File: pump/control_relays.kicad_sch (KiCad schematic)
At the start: 16 parts, among them K1 G5LE-1, K2 G5LE-1, Q1 PNP, Q2 PNP, U1 LTV-817S, U2 LTV-817S

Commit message: -:
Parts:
- D1: footprint Diode_SMD:D_MELF -> Diode_SMD:D_0805_2012Metric_Pad1.15x1.40mm_HandSolder
- D2: LCSC (none) -> C64898; PartNo SM4007PL -> (none)
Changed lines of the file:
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@@
 			)
 		)
-		(property "Footprint" "Diode_SMD:D_MELF"
+		(property "Footprint" "Diode_SMD:D_0805_2012Metric_Pad1.15x1.40mm_HandSolder"
 			(at 135.255 120.65 0)
 			(effects
@@
 			)
 		)
-		(property "Field7" ""
+		(property "LCSC" "C64898"
 			(at 139.7 57.15 90)
 			(effects
-				(font
-					(size 1.27 1.27)
-				)
-				(hide yes)
-			)
-		)
-		(property "PartNo" "SM4007PL"
-			(at 139.7 57.15 90)
-			(effects

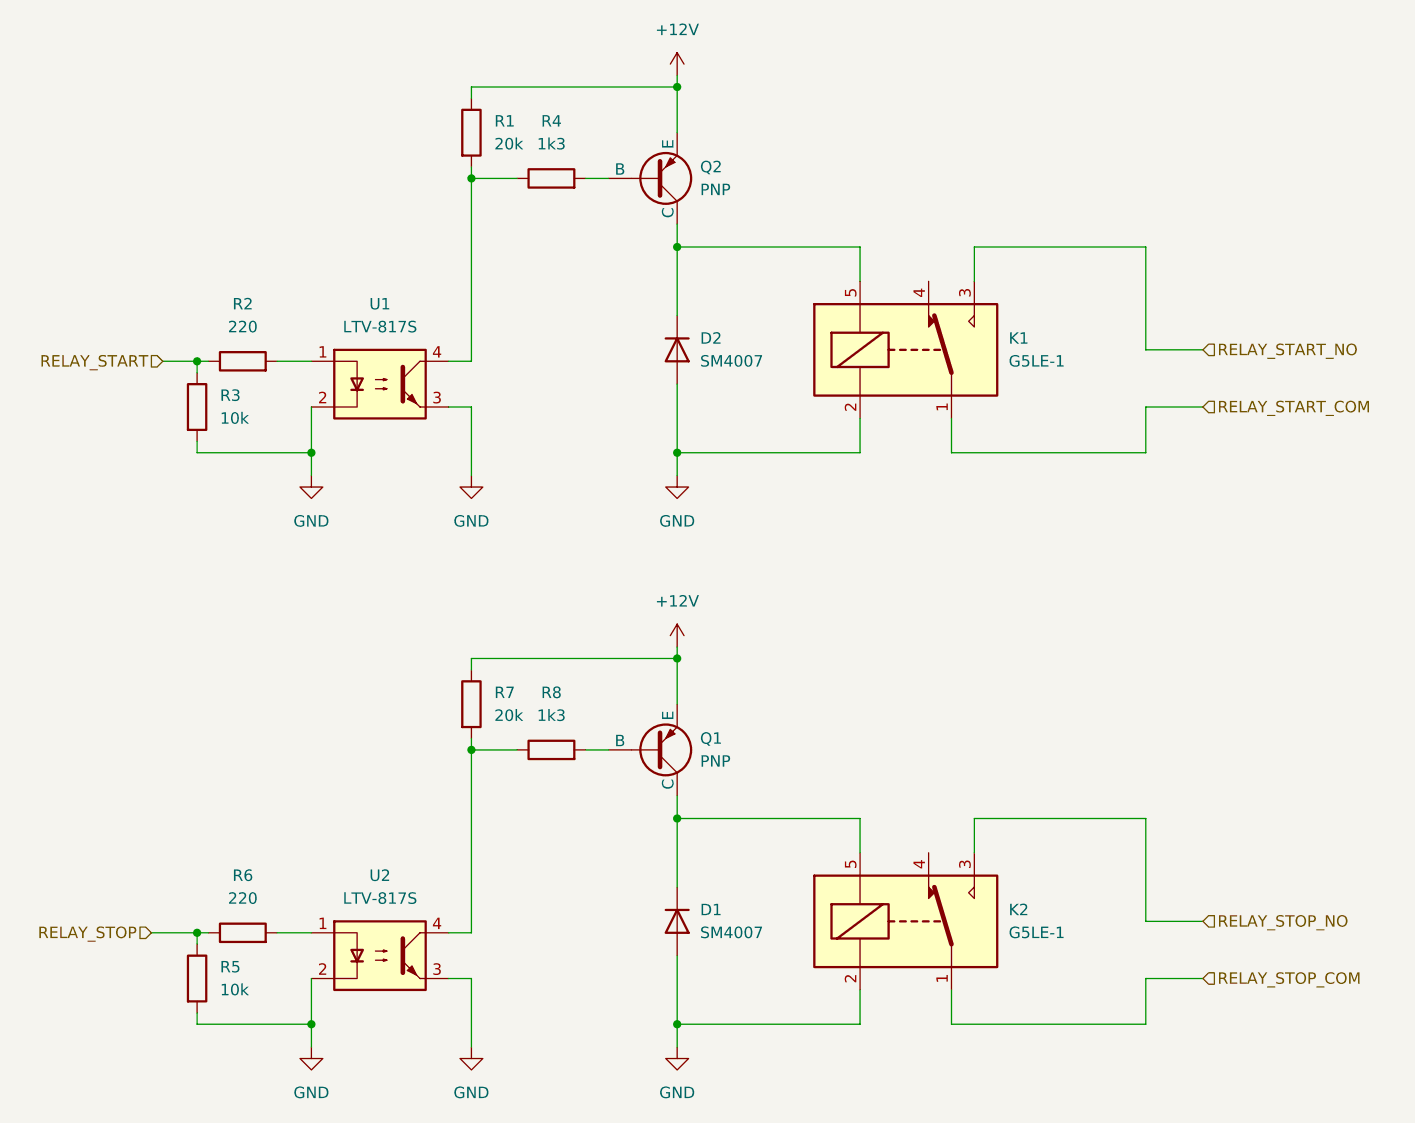
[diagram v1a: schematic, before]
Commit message: finished control relays schematic and footprints
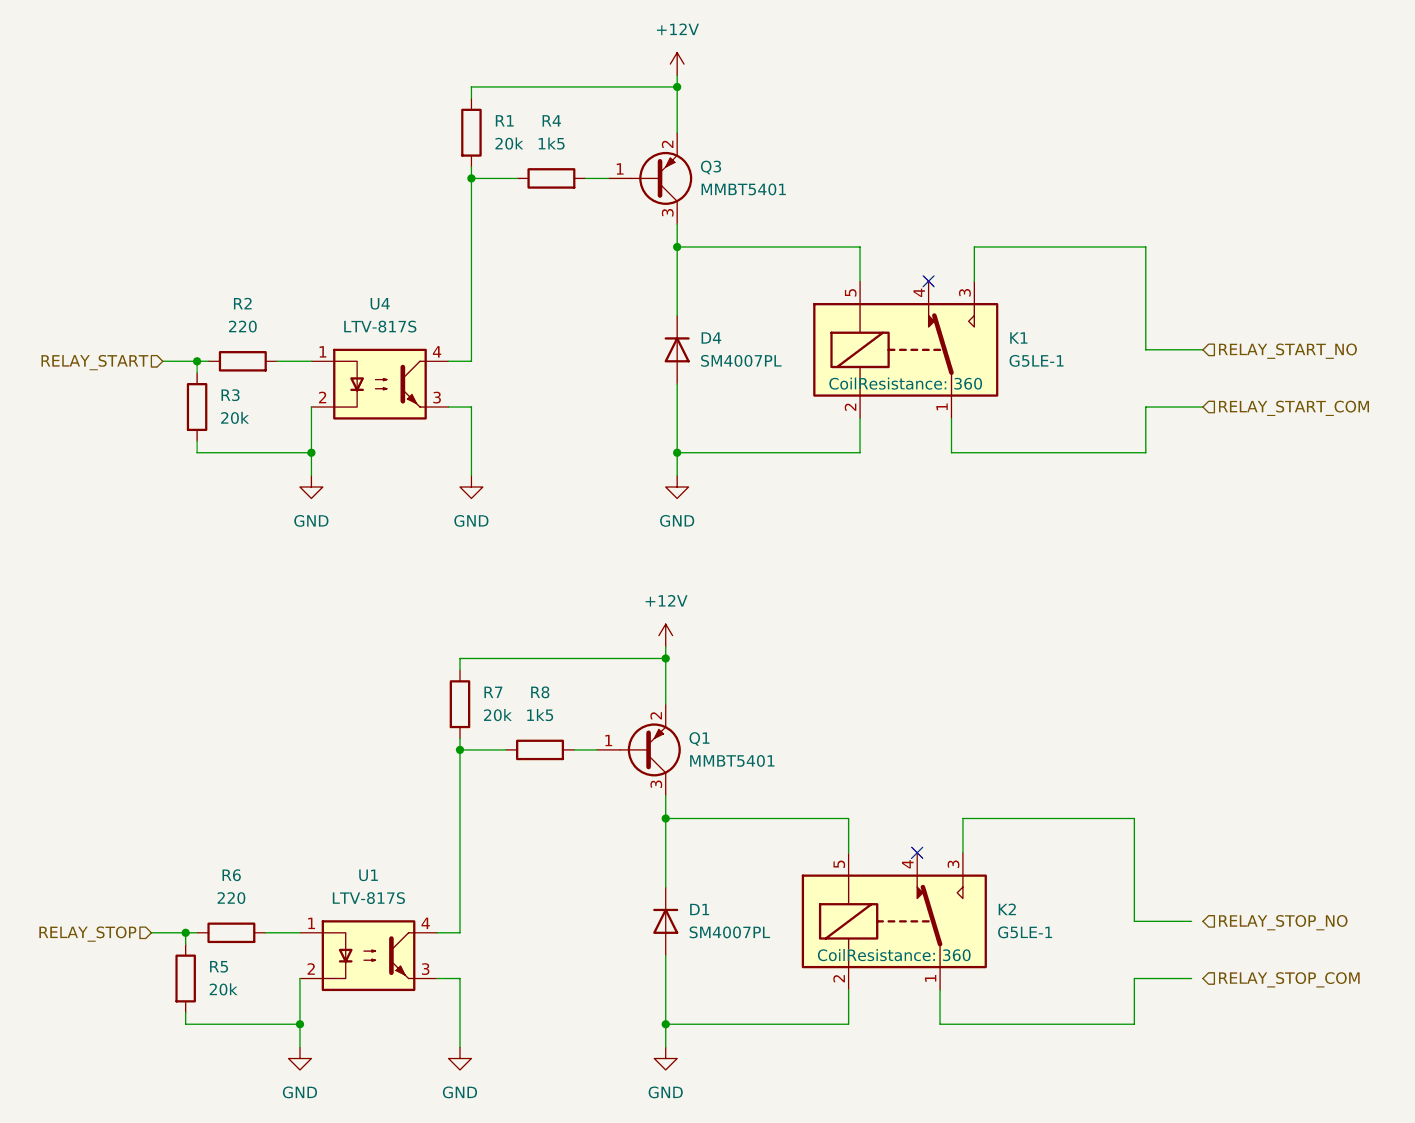
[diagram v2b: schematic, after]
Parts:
- removed D1: SM4007, Diode_SMD:D_0805_2012Metric_Pad1.15x1.40mm_HandSolder, symbol Diode:SM4007
- removed D2: SM4007, Diode_SMD:D_MELF, symbol Diode:SM4007
- removed Q1, Q2: PNP, symbol Simulation_SPICE:PNP
- removed U2: LTV-817S, Package_DIP:SMDIP-4_W9.53mm, symbol Isolator:LTV-817S
- added D1, D4: SM4007PL, pump:SM4007PL, symbol pump:SM4007PL
- added Q1, Q3: MMBT5401, Package_TO_SOT_SMD:SOT-23, symbol Transistor_BJT:MMBTA56
- added U4: LTV-817S, Package_DIP:SMDIP-4_W9.53mm, symbol Isolator:LTV-817S
- K1, K2: CoilResistance (none) -> 360; Mouser (none) -> 653-G5LE-14-ASIDC12
- R1, R7: footprint (none) -> Resistor_SMD:R_0402_1005Metric; LCSC (none) -> C25765; PartNo (none) -> 0402WGF2002TCE
- R2, R6: footprint (none) -> Resistor_SMD:R_0805_2012Metric; LCSC (none) -> C17557; PartNo (none) -> 0805W8F2200T5E
- R3, R5: value 10k -> 20k; footprint (none) -> Resistor_SMD:R_0402_1005Metric; LCSC (none) -> C25765; PartNo (none) -> 0402WGF2002TCE
- R4, R8: value 1k3 -> 1k5; footprint (none) -> Resistor_SMD:R_0805_2012Metric; LCSC (none) -> C4310; PartNo (none) -> 0805W8F1501T5E
- U1: LCSC (none) -> C109227; PartNo (none) -> LTV-817S-TA1-C
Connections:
- net +12V: now also Q1.2 (E), Q3.2 (E)
- net GND: now also D1.2 (A), D4.2 (A), U4.2, U4.3
- net RELAY_STOP_COM: no longer K2.1
- net RELAY_STOP_NO: no longer K2.3
- net at K1.5: now also D4.1 (K), Q3.3 (C)
- net at R4.2: now also Q3.1 (B)
- net at K2.5: now also D1.1 (K), Q1.3 (C)
- net at R6.2: now also U1.1
- net at R1.2, R4.1: now also U4.4; no longer U1.4
- net at R8.2: now also Q1.1 (B)
- net at R2.2: now also U4.1; no longer U1.1
- net at R7.2, R8.1: now also U1.4
- no-connect marks 0 -> 2
